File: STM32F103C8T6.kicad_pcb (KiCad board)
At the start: 2 copper layers, 40 x 33 mm, 33 parts, among them J1 USB_B_Micro, J2 Conn_01x04_Pin, J3 Conn_01x04_Pin, J4 Conn_01x04_Pin, SW1 SW_SPDT, U1 STM32F103C8T6, U2 AMS1117-3.3, Y1 16MHz

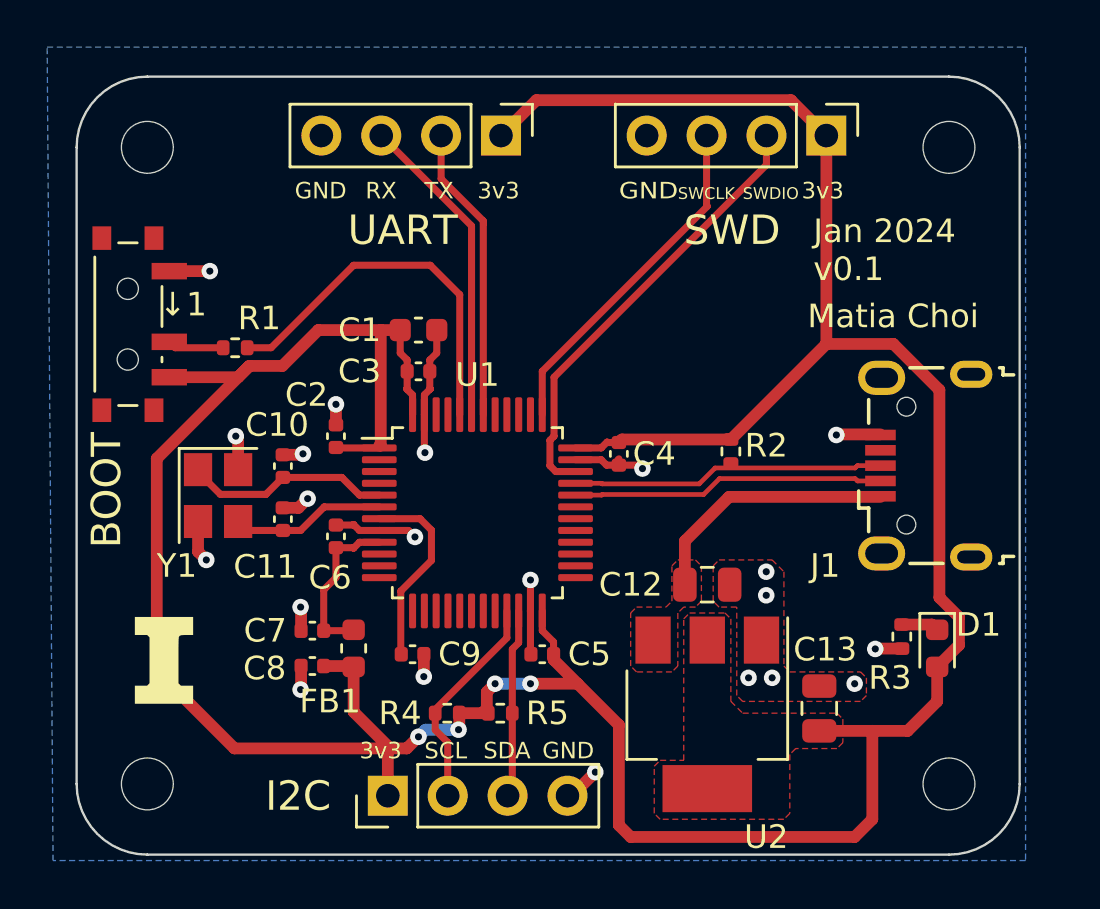
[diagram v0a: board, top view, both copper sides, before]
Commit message: updated footprints to ones which have stocks at JLCPCB
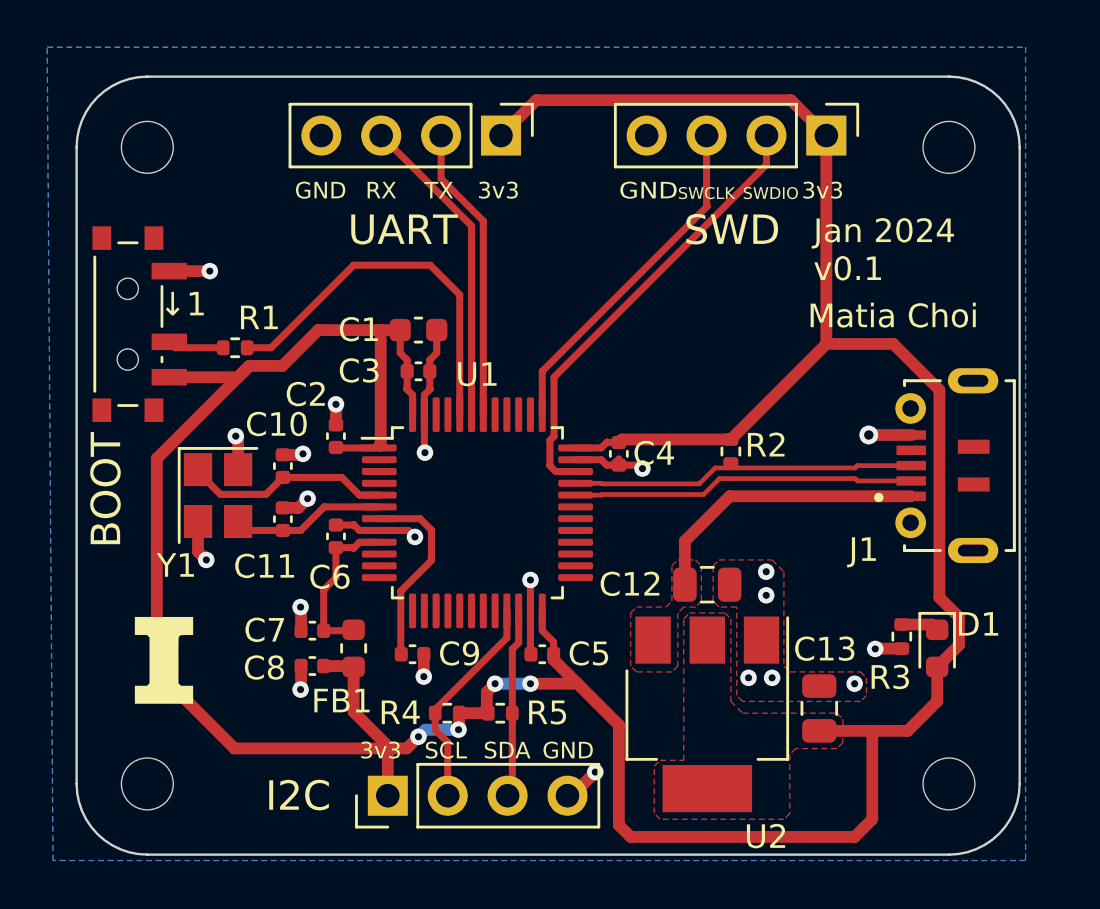
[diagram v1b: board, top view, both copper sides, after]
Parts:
- J1: value USB_B_Micro -> MICROXNJ; footprint Connector_USB:USB_Micro-B_Wuerth_629105150521 -> project_footprints:SHOUHAN_MICROXNJ
- moved J1 3.78 mm to (127.8, 83.0), turned to -90 degrees
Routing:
- net /USB_D-: track 13.3 -> 14.6 mm
- net /USB_D+: track 13.3 -> 14.6 mm
- net VBUS: track 10.9 -> 12.2 mm
